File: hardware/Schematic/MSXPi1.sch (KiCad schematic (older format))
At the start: 46 parts, among them J1 Raspberry_Pi_Zero_2_3, J2 JTAG, J3 Conn_02x07_Odd_Even, J4 Conn_02x06_Odd_Even, J5 SJ-2509N, P1 MSX_CONNECTOR, U1 EPM3064ALC44-10, U2 AT28C256-15PU

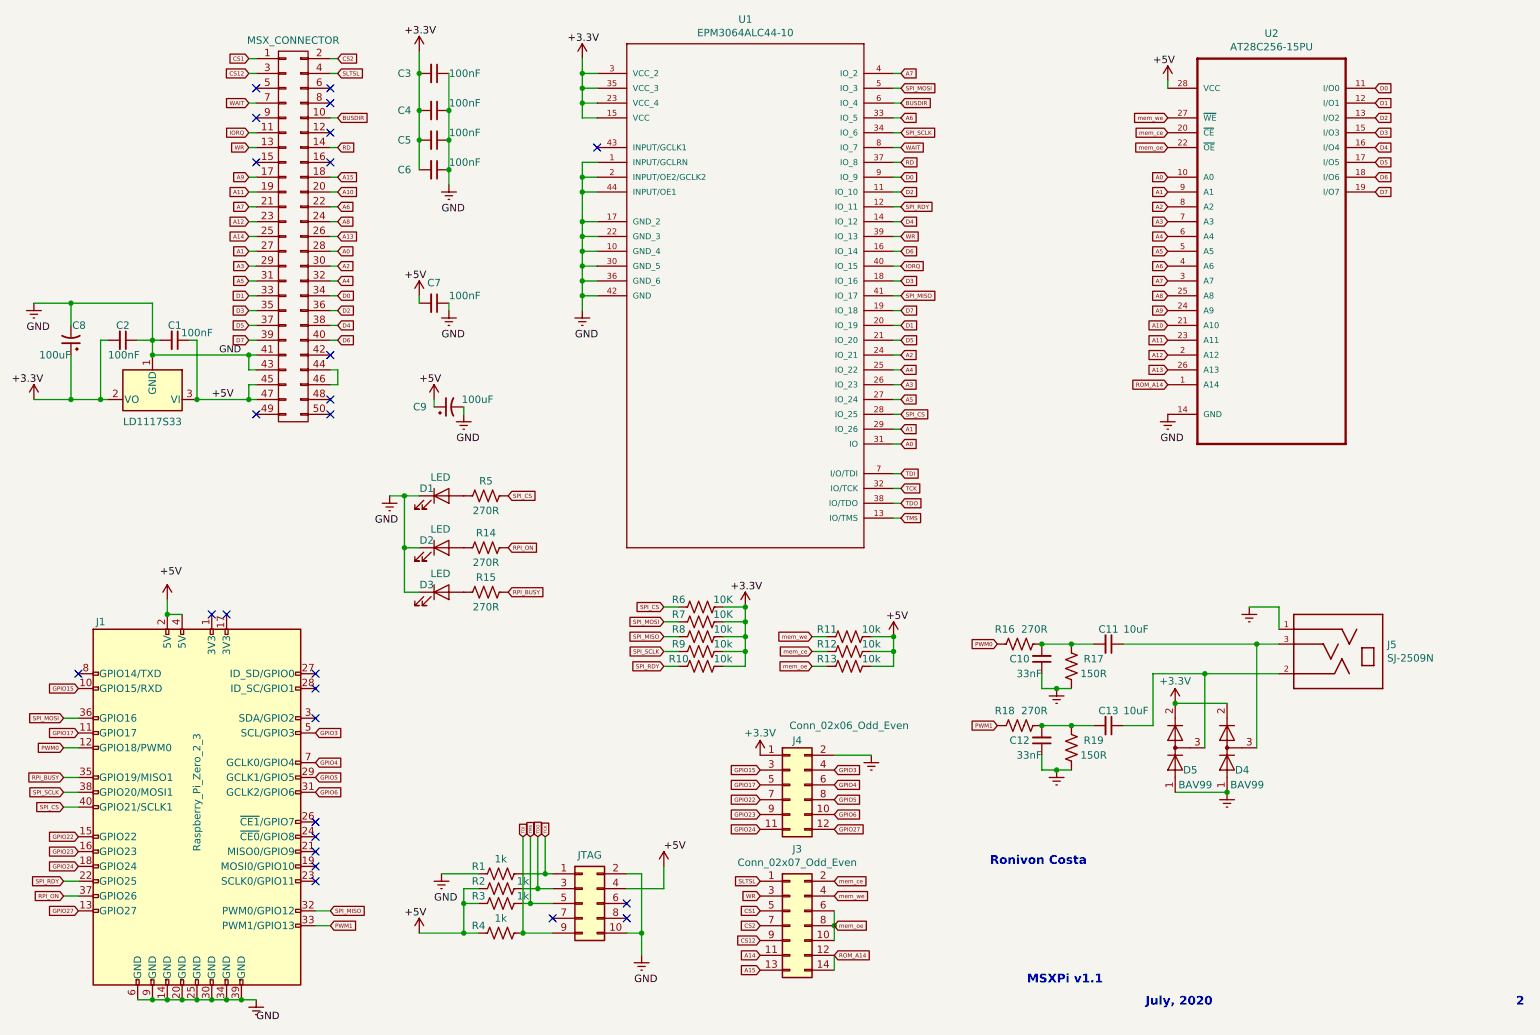
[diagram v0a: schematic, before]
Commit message: PCB v1.1 Rev.3 - Replaced CPLD by TQFP package (epm3064atc44-10n).
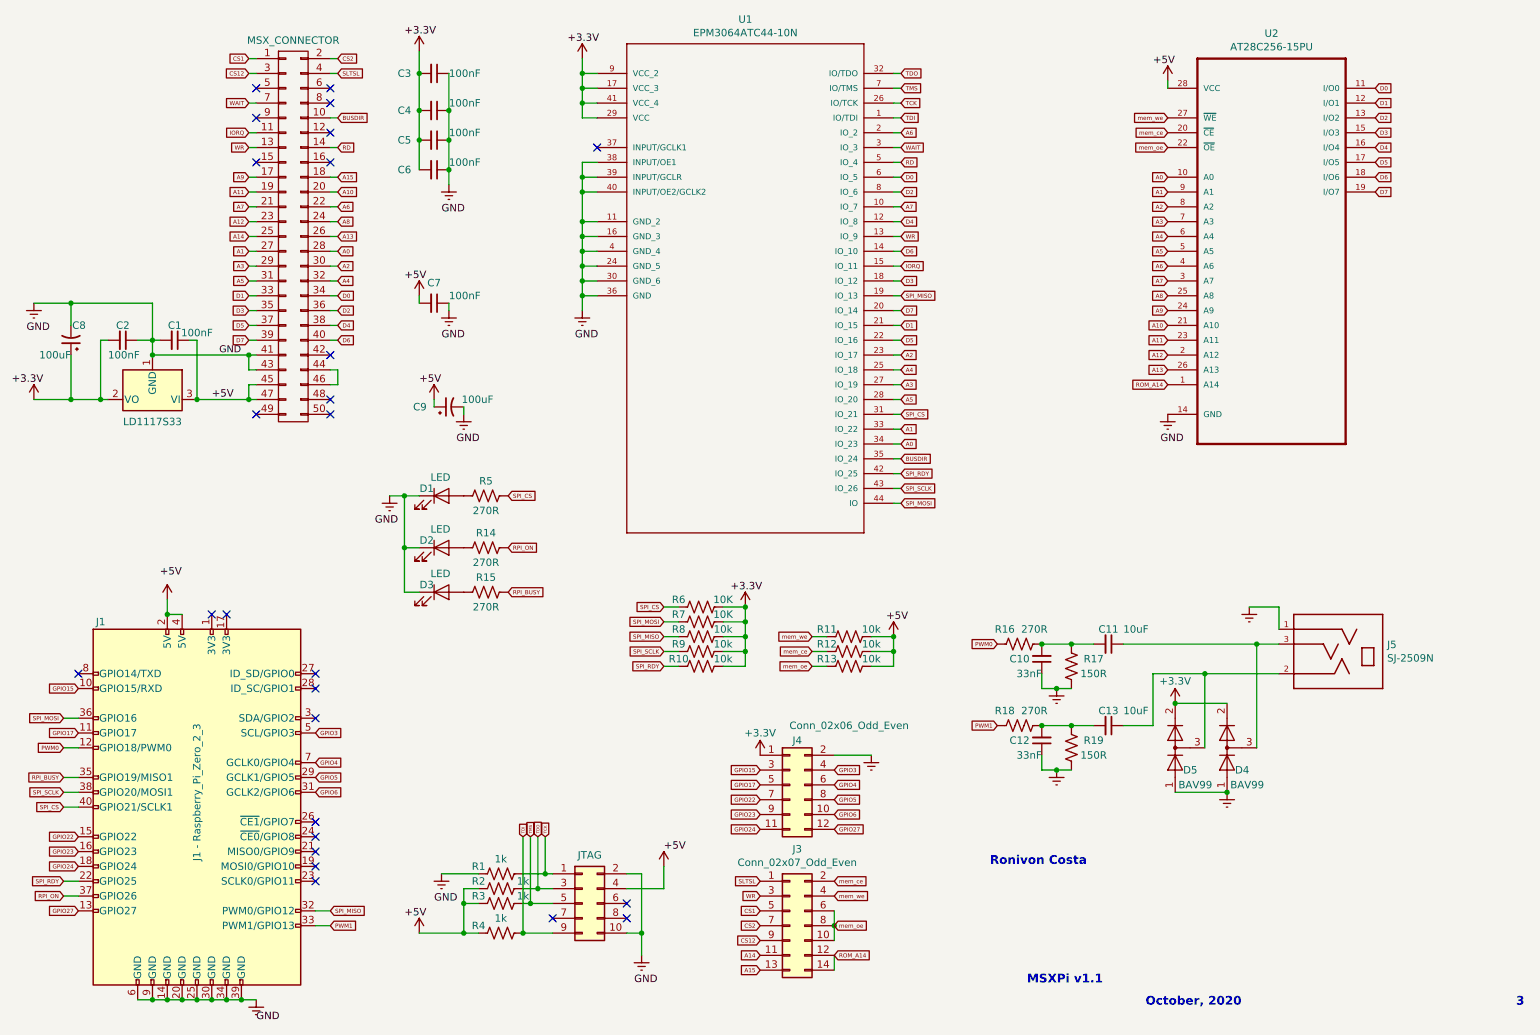
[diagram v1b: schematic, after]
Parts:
- removed U1: EPM3064ALC44-10, MyFootprints:PLCC127P1765X1765X457-44N, symbol EPM3064ALC44-10:EPM3064ALC44-10
- added U1: EPM3064ATC44-10N, MyFootprints:QFP80P1200X1200X120-44N, symbol EPM3064ATC4410:EPM3064ATC44-10N
- J1: value Raspberry_Pi_Zero_2_3 -> J1 - Raspberry_Pi_Zero_2_3
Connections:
- net +3V3: now also U1.17 (VCC_3), U1.29 (VCC), U1.41 (VCC_4), U1.9 (VCC_2)
- net A0: now also U1.34 (IO_23)
- net A1: now also U1.33 (IO_22)
- net A2: now also U1.23 (IO_17)
- net A3: now also U1.27 (IO_19)
- net A4: now also U1.25 (IO_18)
- net A5: now also U1.28 (IO_20)
- net A6: now also U1.2 (IO_2)
- net A7: now also U1.10 (IO_7)
- net BUSDIR: now also U1.35 (IO_24)
- net D0: now also U1.6 (IO_5)
- net D1: now also U1.21 (IO_15)
- net D2: now also U1.8 (IO_6)
- net D3: now also U1.18 (IO_12)
- net D4: now also U1.12 (IO_8)
- net D5: now also U1.22 (IO_16)
- net D6: now also U1.14 (IO_10)
- net D7: now also U1.20 (IO_14)
- net GNDREF: now also U1.11 (GND_2), U1.16 (GND_3), U1.24 (GND_5), U1.30 (GND_6), U1.36 (GND), U1.38 (INPUT/OE1), U1.39 (INPUT/GCLR), U1.4 (GND_4), U1.40 (INPUT/OE2/GCLK2)
- net IORQ: now also U1.15 (IO_11)
- net RD: now also U1.5 (IO_4)
- net SPI_CS: now also U1.31 (IO_21)
- net SPI_MISO: now also U1.19 (IO_13)
- net SPI_MOSI: now also U1.44 (IO)
- net SPI_RDY: now also U1.42 (IO_25)
- net SPI_SCLK: now also U1.43 (IO_26)
- net TCK: now also U1.26 (IO/TCK)
- net TDI: now also U1.1 (IO/TDI)
- net TDO: now also U1.32 (IO/TDO)
- net TMS: now also U1.7 (IO/TMS)
- net WAIT: now also U1.3 (IO_3)
- net WR: now also U1.13 (IO_9)
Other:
- note added: "3"
- note added: "October, 2020"
- note removed: "2"
- note removed: "July, 2020"
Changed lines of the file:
@@
 P 1750 6300
 F 0 "J1" H 1100 7550 50  0000 C CNN
-F 1 "Raspberry_Pi_Zero_2_3" V 1750 6400 50  0000 C CNN
+F 1 "J1 - Raspberry_Pi_Zero_2_3" V 1750 6400 50  0000 C CNN
 F 2 "Connector_PinHeader_2.54mm:PinHeader_2x20_P2.54mm_Vertical" H 1750 6300 50  0001 C CNN
 F 3 "https://www.raspberrypi.org/documentation/hardware/raspberrypi/schematics/rpi_SCH_3bplus_1p0_reduced.pdf" H 1750 6300 50  0001 C CNN
@@
 MSXPi v1.1
 Text Notes 8150 7650 0    59   ~ 12
-July, 2020
+October, 2020
 Text Notes 10650 7650 0    59   ~ 12
-2
+3
 Text Notes 7100 6700 0    59   ~ 12
 Ronivon Costa
-$Comp
-L EPM3064ALC44-10:EPM3064ALC44-10 U1
-U 1 1 5F21A6E6
-P 5450 2750
-F 0 "U1" H 5450 4515 50  0000 C CNN
-F 1 "EPM3064ALC44-10" H 5450 4424 50  0000 C CNN
-F 2 "MyFootprints:PLCC127P1765X1765X457-44N" H 5450 2750 50  0001 L BNN
-F 3 "Altera" H 5450 2750 50  0001 L BNN
-F 4 "1549412" H 5450 2750 50  0001 L BNN "Field4"
-F 5 "51R0503" H 5450 2750 50  0001 L BNN "Field5"
-F 6 "EPM3064ALC44-10" H 5450 2750 50  0001 L BNN "Field6"
-F 7 "44-PLCC" H 5450 2750 50  0001 L BNN "Field7"
-	1    5450 2750
-	1    0    0    -1
-$EndComp
 Text GLabel 6500 2750 2    28   Input ~ 0
 D3
@@
 Wire Wire Line
 	6450 3750 6500 3750
-Text GLabel 6500 1650 2    28   Input ~ 0
-A6
-Wire Wire Line
-	6450 1650 6500 1650
-Wire Wire Line
-	6450 1750 6500 1750
-Text GLabel 6500 1450 2    28   Input ~ 0
-SPI_MOSI
 Text GLabel 6500 2150 2    28   Input ~ 0
 D2
-Text GLabel 6500 2250 2    28   Input ~ 0
+Text GLabel 6500 4050 2    28   Input ~ 0
 SPI_RDY
 Text GLabel 6500 2350 2    28   Input ~ 0
@@
 Wire Wire Line
 	6450 2050 6500 2050
-Text GLabel 6500 1550 2    28   Input ~ 0
-BUSDIR
 Wire Wire Line
 	6450 1450 6500 1450
-Text GLabel 6500 1350 2    28   Input ~ 0
+Text GLabel 6500 2250 2    28   Input ~ 0
 A7
 Wire Wire Line
@@
 Text GLabel 8300 1850 0    28   Input ~ 0
 mem_oe
-Text GLabel 6500 1750 2    28   Input ~ 0
-SPI_SCLK
-Text GLabel 6500 4050 2    28   Input ~ 0
+Text GLabel 6500 1650 2    28   Input ~ 0
 TDI
-Text GLabel 6500 4150 2    28   Input ~ 0
+Text GLabel 6500 1550 2    28   Input ~ 0
 TCK
-Text GLabel 6500 4250 2    28   Input ~ 0
+Text GLabel 6500 1350 2    28   Input ~ 0
 TDO
-Text GLabel 6500 4350 2    28   Input ~ 0
+Text GLabel 6500 1450 2    28   Input ~ 0
 TMS
 Wire Wire Line
@@
 Wire Wire Line
 	6450 4250 6500 4250
-Wire Wire Line
-	6450 4350 6500 4350
 $Comp
 L power:+3.3V #PWR02
@@
 	4350 2850 4450 2850
 NoConn ~ 4450 1850
-Wire Wire Line
-	6450 1550 6500 1550
-Text GLabel 6500 1950 2    28   Input ~ 0
-RD
-Text GLabel 6500 1850 2    28   Input ~ 0
-WAIT
-Wire Wire Line
-	6450 1850 6500 1850
 Text GLabel 2100 1550 0    28   Input ~ 0
 WAIT
@@
 Wire Wire Line
 	2650 1350 2700 1350
-Wire Wire Line
-	6450 1950 6500 1950
 NoConn ~ 2650 1750
 Text GLabel 2700 1250 2    28   Input ~ 0
@@
 	1    0    0    -1
 $EndComp
+$Comp
+L EPM3064ATC4410:EPM3064ATC44-10N U1
+U 1 1 5F857D7E
+P 5450 2650
+F 0 "U1" H 5450 4315 50  0000 C CNN
+F 1 "EPM3064ATC44-10N" H 5450 4224 50  0000 C CNN
+F 2 "MyFootprints:QFP80P1200X1200X120-44N" H 5450 2650 50  0001 L BNN
+F 3 "1549417" H 5450 2650 50  0001 L BNN
+F 4 "EPM3064ATC44-10N" H 5450 2650 50  0001 L BNN "Field4"
+F 5 "44-TQFP" H 5450 2650 50  0001 L BNN "Field5"
+F 6 "51R0505" H 5450 2650 50  0001 L BNN "Field6"
+F 7 "Altera" H 5450 2650 50  0001 L BNN "Field7"
+	1    5450 2650
+	1    0    0    -1
+$EndComp
+Wire Wire Line
+	6450 1950 6500 1950
+Wire Wire Line
+	6450 1850 6500 1850
+Text GLabel 6500 1850 2    28   Input ~ 0
+WAIT
+Text GLabel 6500 1950 2    28   Input ~ 0
+RD
+Wire Wire Line
+	6450 1550 6500 1550
+Text GLabel 6500 4150 2    28   Input ~ 0
+SPI_SCLK
+Text GLabel 6500 3950 2    28   Input ~ 0
+BUSDIR
+Text GLabel 6500 4250 2    28   Input ~ 0
+SPI_MOSI
+Wire Wire Line
+	6450 1750 6500 1750
+Wire Wire Line
+	6450 1650 6500 1650
+Text GLabel 6500 1750 2    28   Input ~ 0
+A6
+Wire Wire Line
+	6450 3950 6500 3950
 $EndSCHEMATC
